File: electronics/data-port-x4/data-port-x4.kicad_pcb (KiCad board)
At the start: 4 copper layers, 108 x 24 mm, 114 parts, among them J1 LEAD, J101 PORT1, J102 AUX1, J201 PORT2, J202 AUX2, J301 PORT3, J302 AUX3, J401 PORT4, J402 AUX4, Q1 2N7002, Q2 2N7002, Q3 2N7002, U1 USB2514B-AEZC-TR, U101 TPS2553DBVR-1, U102 INA226AIDGSR, U103 USBLC6-2SC6, U2 TCA6408ARGTR, U201 TPS2553DBVR-1, U202 INA226AIDGSR, U203 USBLC6-2SC6, U3 AP2112K-3.3TRG1, U301 TPS2553DBVR-1, U302 INA226AIDGSR, U303 USBLC6-2SC6, U4 USBLC6-2SC6, U401 TPS2553DBVR-1, U402 INA226AIDGSR, U403 USBLC6-2SC6, U5 USBLC6-2SC6, U6 TCA6408ARGTR, Y1 X322524MSB4SI

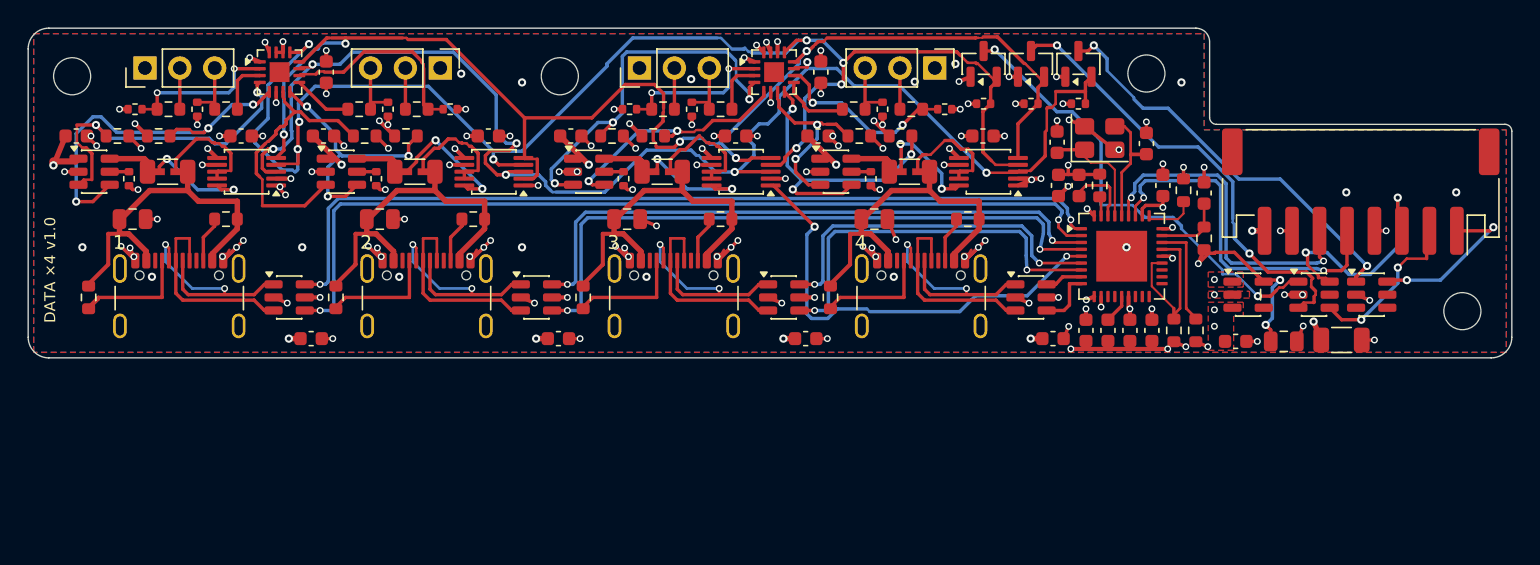
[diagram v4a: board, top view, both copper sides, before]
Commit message: DATA ×4: 100 × 28 mm, the lead on the right edge
The board shrinks to 100 mm (JLC's 4-layer offer, no engineering fee)
and grows 4 mm towards the rear: 100 × 28, no notch.  The four USB-C,
their ports, pairs and ESD flow-through stay exactly where they were
(the layout moves 4 mm off the rear edge as a whole, DY in design.py).
J1 (PH 8, side entry) moves to the right edge, its mouth at drawer x 115,
pin 1 at the front; its lead ESDs face its pins, U4 turned 270°, U5 level
with pin 1; C1 by its +5V pin; U3 behind it, turned 180° with its VIN,
EN and GND islands (the same shapes) and a +3V3 bump in In2 under its
output.  H1-H3 keep their drawer spots, H4 moves to the rear-right corner
(96.8, 3.5): the drawer's one set of DATA ×4 bosses, the v2's too.

Routing against the 108 mm board: the upstream pair goes from 26 / 25 mm
to 15 / 15 mm, two vias each as before; the 16 port pair nets are
unchanged to 0.05 mm and to the via; no B.Cu pair segment over In2's
+3V3 (both notches kept); the +5V neck under the hub stays 2.44 mm with
no via; the LDO islands are as large (EN 4.7 mm² against 4.4).  Router
copper 721 mm and 91 vias against 799 mm and 93.  Port 3's INA226 A1
strap gets a via of its own (its fan-out had no room, Freerouting missed
it now and then).  Nothing ends up worse.

ERC 0, DRC 0, parity 0, 0 unconnected (the best of seven routing
variants on the Mac and zephyrbox).  The review's CPL audit agrees on all
106 parts.  rack.yaml carries the new size, holes and J1 (`lead`, the
notch and `ph` gone); the viewer's stand-in shows J1 on the right edge
and brings the lead up beside the board.  The bare PCB is priced at the
bay node's 4-layer offer ($13.20 for 5) until the JLC-cost owner
re-quotes it: about $85 for 5 with 2 assembled instead of $104.  The
drawer's window and the new H4 boss are the Mechanics session's.

Co-Authored-By: Claude Opus 5.5 <noreply@anthropic.com>
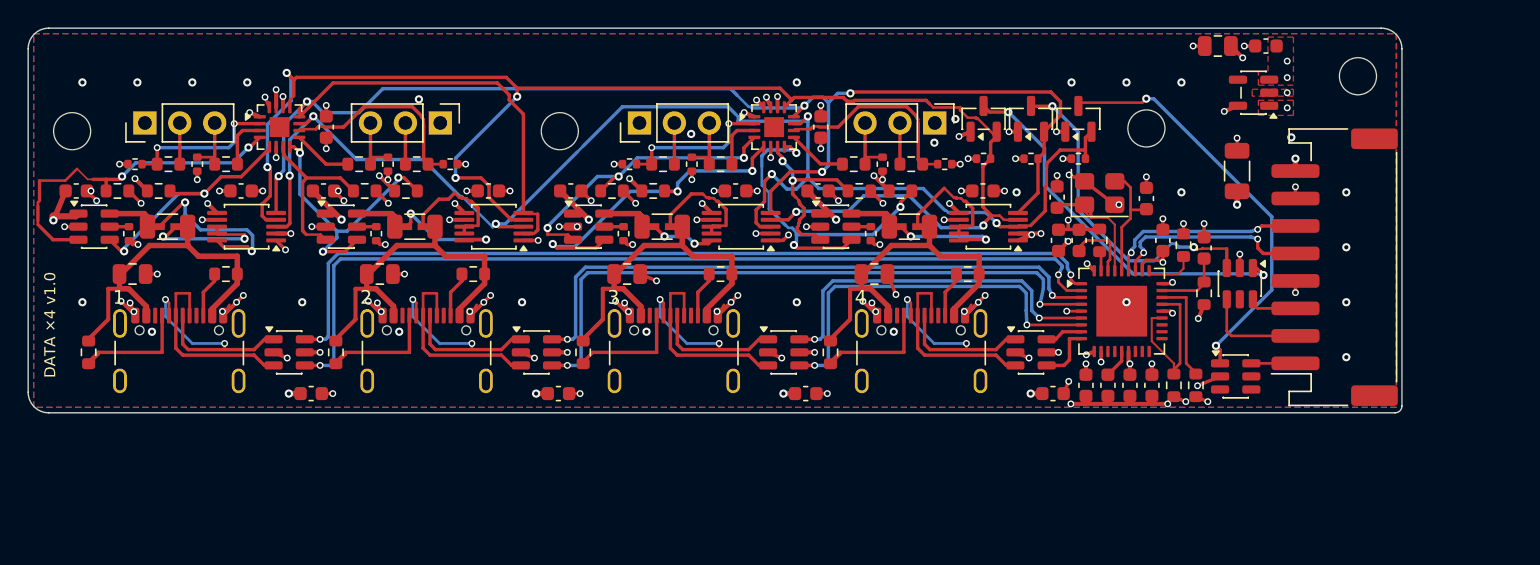
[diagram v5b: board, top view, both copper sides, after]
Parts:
- moved C3 22.0 mm to (86.6, 1.30), turned to 180 degrees
- moved C2 21.6 mm to (90.1, 1.30), turned to 180 degrees
- moved H4 18.7 mm to (96.8, 3.50)
- moved U3 14.7 mm to (89.2, 4.70), turned to 180 degrees
- moved C1 14.5 mm to (88.0, 10.4), turned to 90 degrees
- moved U5 11.6 mm to (87.9, 25.4)
- moved J1 5.82 mm to (95.1, 17.4), turned to 90 degrees
- moved U4 5.46 mm to (88.2, 18.6), turned to -90 degrees
- moved C10 4.00 mm to (81.8, 26.0)
- moved C101 4.00 mm to (3.50, 11.8)
- moved C103 4.00 mm to (15.5, 11.8)
- moved C104 4.00 mm to (20.6, 26.6)
- moved C11 4.00 mm to (77.0, 26.0)
- moved C12 4.00 mm to (80.2, 26.0)
- moved C13 4.00 mm to (85.6, 16.0)
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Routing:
- net +3V3: track 89.3 -> 49.4 mm, vias 51 -> 52
- net SCL: track 99.1 -> 118.7 mm
- net /Hub/LEAD_SDA: track 17.5 -> 3.56 mm, vias 2 -> 0
- net /Hub/UP_DN: track 26.2 -> 14.7 mm
- net /Hub/UP_DP: track 24.7 -> 14.5 mm
- net PORT1_FLT_N: track 27.4 -> 17.9 mm, vias 3 -> 2
- net /Hub/BUS_SCL: track 33.3 -> 24.4 mm
- net /Hub/LEAD_INT: track 12.1 -> 3.21 mm, vias 2 -> 0
- net PORT2_EN: track 20.4 -> 12.7 mm
- net PORT3_FLT_N: track 18.0 -> 24.4 mm, vias 2 -> 3
- net /Hub/BUS_SDA: track 33.9 -> 28.0 mm
- net PORT3_EN: track 28.1 -> 22.5 mm
- net SDA: track 106.6 -> 111.6 mm, vias 8 -> 6
- net /Port 1/PORT1_SNS_P: track 8.28 -> 13.1 mm
- net /Hub/LEAD_SCL: track 12.0 -> 7.46 mm, vias 2 -> 0
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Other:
- board size 108 x 24 mm -> 100 x 28 mm

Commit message: DATA ×4: 100 × 37 mm, J1 at the rear end of the right edge, no fourth hole
On top of 1c0dfbd (100 × 28, J1 centred on the right edge):
- 100 × 37 mm, as deep as the v2: 13 mm deeper than the layout's 24 mm frame, still under JLC's 100 mm
  4-layer offer.
- J1 at the rear end of the right edge: mouth at drawer x 115, pins at drawer y 176–190, the plug
  (y ≈ 174–192) over the drawer's side window and clear of the v2's front-right boss. The LDO block
  and its islands sit in the corner behind it, unchanged.
- No fourth hole: v1 sits on H1–H3, unchanged in drawer coordinates, and on the front ledges. The
  plug forces stay in the board's plane. The drawer (2a3309b) already has no boss there.
- The upstream pair runs 45° from J1's vias into the hub's notch, and In2's +3V3 edge follows the
  diagonal: 16.7 / 17.2 mm pad to pin, 2 vias (1c0dfbd: 14.7 / 14.5). The lead's ESDs line up with
  J1's pins (flow-through). C13 and R2 move north of R5.

Against 1c0dfbd, unchanged or better:
- port pairs, their ESDs and the B.Cu lanes unchanged;
- every pair on one reference plane end to end (+5V on In2);
- +5V neck 2.45 mm (2.34);
- LDO islands unchanged (1.31 / 1.31 / 4.72 mm²);
- router copper 1580 mm (1612), signal vias 76 (79): the best of seven Freerouting variants. The 59
  extra GND vias are the larger pours' stitching.
- ERC 0, DRC 0, parity 0, 0 unconnected.
- CPL audit: 99 parts pass. The flags are the same 7 as 1c0dfbd's, positions agree: the USB4105s'
  symmetric pin 1, and the C1 / J1 / U3 land residuals against EasyEDA.

Worse:
- the upstream pair is 2.0 / 2.7 mm longer. J1's pins moved 6.4 mm to the rear, and a 45° route
  cannot do better (≈ 15 ps at 480 Mb/s, beside a 45 cm lead).
- its D+/D− mismatch is 0.53 mm (0.23). That is under the 1.27 mm usual for USB 2.0, and the
  downstream pairs already differ by 2.2 mm.

JLC's bare PCB at 100 × 37 (calculator, 2026-10-20): $13.10 for 5 ($8.00 offer + lead-free HASL
$5.10, no deburring line), $19.20 / $53.80 / $73.40 f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
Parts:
- removed H4: PT2.6, MountingHole:MountingHole_2.7mm_M2.5
- moved C101 9.00 mm to (3.50, 20.9)
- moved C103 9.00 mm to (15.5, 20.9)
- moved C201 9.00 mm to (21.5, 20.9)
- moved C203 9.00 mm to (33.5, 20.9)
- moved C301 9.00 mm to (39.5, 20.9)
- moved C303 9.00 mm to (51.5, 20.9)
- moved C401 9.00 mm to (57.5, 20.9)
- moved C403 9.00 mm to (69.5, 20.9)
- moved R102 9.00 mm to (6.50, 20.9)
- moved R103 9.00 mm to (9.50, 20.9)
- moved R202 9.00 mm to (24.5, 20.9)
- moved R203 9.00 mm to (27.5, 20.9)
- moved R302 9.00 mm to (42.5, 20.9)
- moved R303 9.00 mm to (45.5, 20.9)
- moved R402 9.00 mm to (60.5, 20.9)
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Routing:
- net SDA: track 111.6 -> 97.6 mm
- net SCL: track 118.7 -> 111.3 mm, vias 5 -> 6
- net INT: track 99.0 -> 106.4 mm
- net /Hub/BUS_SDA: track 28.0 -> 22.4 mm
- net /Hub/HUB_RST_N: track 5.22 -> 10.5 mm
- net /Port 1/PORT1_SNS_P: track 13.1 -> 8.63 mm
- net /Hub/LEAD_SCL: track 7.46 -> 3.21 mm
- net PORT1_EN: track 25.5 -> 21.7 mm
- net /Port 4/PORT4_SNS_P: track 8.54 -> 4.81 mm
- net PORT4_FLT_N: track 26.1 -> 22.4 mm
- net /Hub/UP_DP: track 14.5 -> 17.2 mm
- net /Hub/UP_DN: track 14.7 -> 16.7 mm
- net PORT2_FLT_N: track 20.5 -> 18.7 mm
- net /Hub/BUS_SCL: track 24.4 -> 22.7 mm
- net /Hub/BUS_INT: track 30.4 -> 28.8 mm
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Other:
- board size 100 x 28 mm -> 100 x 37 mm

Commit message: Power pads connect solid on the DATA ×4, the DATA port and the camera pod
The rule from d58f976, applied to the three boards. Each one declares its power nets in design.py:
- DATA ×4: GND, +5V, each port's 5V_SW and VBUS
- DATA port: GND, VBUS
- camera pod: GND, CAM_5V
pcbgen then connects their IC and connector pins solid to the pours. A small part with an end on a
track keeps its reliefs. The .kicad_dru carries both rules.

Now solid:
- DATA ×4: the four receptacles' and J1's GND pins; the hub's, expanders', INA226s', switches' and
  ESDs' GND pins and exposed pads; the LDO's VIN, EN and GND on its islands. Eighteen GND pads the
  pour didn't reach (USB4105 A1/A12/B1/B12 among them) now take it directly, and their tie tracks go
  (25 segments, 11 vias). The ports' 5V_SW and VBUS run in tracks, so their pads don't change.
- DATA port: J1's four GND pins, J2's two, the ESD's GND.
- Camera pod: J1's two GND pins, J2's GND, the AMS1117's GND.

Worst relieved power-net pad, before → after:
- DATA ×4: INA226 GND (U102.7) on 1 spoke, 0.29 mm → solid. Now the worst is a GND decoupling cap or
  pull-down (C201.2, R201.2...) on 1 spoke of 0.40 mm, a signal-level current.
- DATA port: J1's GND pins and U1.2 on 1 spoke, 0.40 mm → solid. Now the worst is C1 / C2 / the shell
  tabs on 3 spokes, 1.20 mm.
- Camera pod: U1.1, J1.5 / J1.7, C1, C3 on 3 spokes, 1.20 mm. Now U1.1 and J1's GND are solid; the
  worst is C1 / C3 on 3 spokes, 1.20 mm.

Same routes re-imported: only GND ties and stitching vias move. ERC/DRC 0, parity 0, 0 unconnected on
all three. CPL and BOM unchanged, so the CPL audit stands. Renders, PDFs and gerbers regenerated.

Co-Authored-By: Claude Opus 5.5 <noreply@anthropic.com>
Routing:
- net GND: track 113.5 -> 101.2 mm, vias 179 -> 170
